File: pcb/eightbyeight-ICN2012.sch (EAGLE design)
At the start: 135 parts, among them J1 USB_MICROSMT+THRUHULE, J2 JTAG_ARM_10PIN, J3 BATTERY, Q1 16MHz, SW1 SWITCH_SPDT, SW2 BRIGHTNESS, U1 MK20DN32VFM5, U2 ICN2026, U3 QMA6981, U4 ICN2026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

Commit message: Update board TODOs
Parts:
- C16: value 470pF -> 47pF
- C6: value 10uF -> 20uF
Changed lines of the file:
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@@
 <part name="C12" library="adafruit" deviceset="C-US" device="C0805" value="10uF"/>
 <part name="C9" library="adafruit" deviceset="C-US" device="C0805" value="10uF"/>
-<part name="C6" library="adafruit" deviceset="C-US" device="C0805" value="10uF"/>
+<part name="C6" library="adafruit" deviceset="C-US" device="C0805" value="20uF"/>
 <part name="GND38" library="SparkFun-Aesthetics" deviceset="GND" device=""/>
 <part name="GND39" library="SparkFun-Aesthetics" deviceset="GND" device=""/>
 <part name="U5" library="SparkFun-PowerIC" deviceset="V_REG_MIC5219" device="3.3V" value="MIC5219 3.3V"/>
-<part name="C16" library="adafruit" deviceset="C-US" device="C0402" value="470pF"/>
+<part name="C16" library="adafruit" deviceset="C-US" device="C0402" value="47pF"/>
 <part name="GND40" library="SparkFun-Aesthetics" deviceset="GND" device=""/>
 <part name="P+1" library="supply1" deviceset="+5V" device=""/>
@@
 -Test a flush-mount USB connector
 -Choose either 3V or 3.3V regulator and make consistent
--Add 5v test pad?</text>
+-Add 5v test pad?
+-Remove pullup resistor on button?</text>
 <text x="129.54" y="358.14" size="10.16" layer="91" align="bottom-center">EightByEight Blinky Badge</text>
 <text x="129.54" y="345.44" size="6.4516" layer="91" align="bottom-center">Copyright 2016 Blinkinlabs, LLC</text>

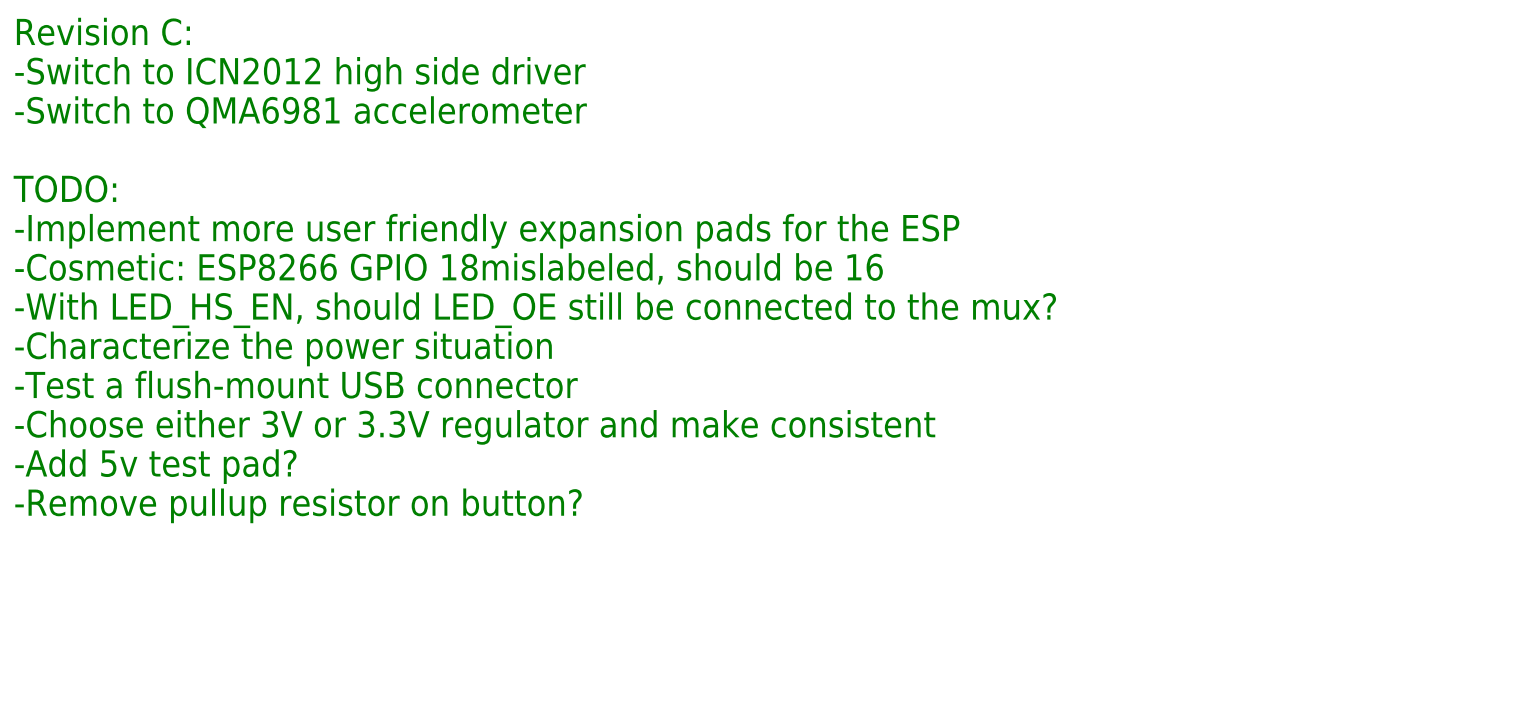
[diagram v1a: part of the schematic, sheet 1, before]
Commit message: Silkscreen tweaks to pcbs
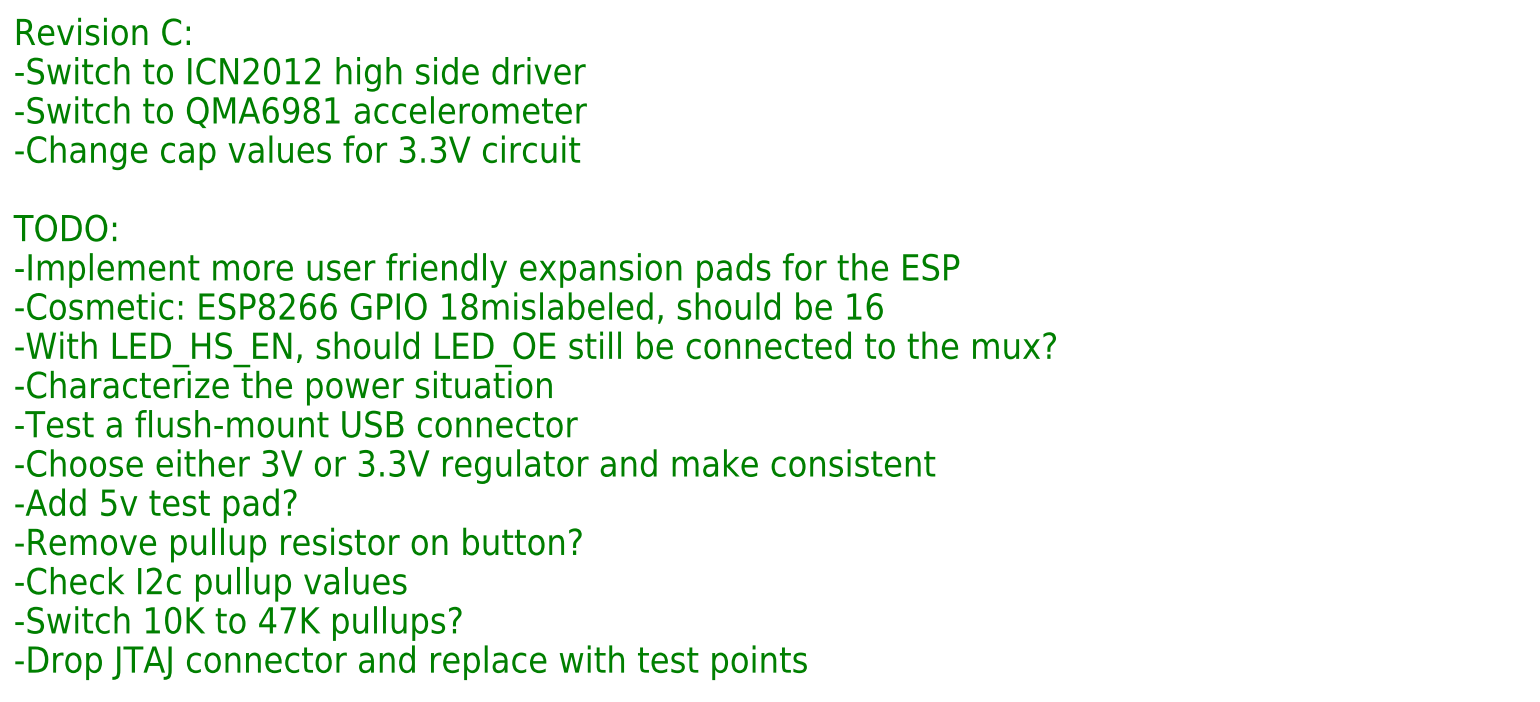
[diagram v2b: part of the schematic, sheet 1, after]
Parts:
- U2, U4: value ICN2026 -> ICN2027
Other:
- note added: "High side (row) driver"
- note removed: "High side (column) driver"
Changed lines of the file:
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@@
 </classes>
 <parts>
-<part name="U2" library="blinkinlabs" deviceset="ICN2026" device=""/>
+<part name="U2" library="blinkinlabs" deviceset="ICN2026" device="" value="ICN2027"/>
 <part name="GND2" library="SparkFun-Aesthetics" deviceset="GND" device=""/>
 <part name="C7" library="adafruit" deviceset="C-US" device="C0402" value="100nF"/>
@@
 <part name="R5" library="adafruit" deviceset="R-US_" device="R0402" value="2k"/>
 <part name="GND8" library="SparkFun-Aesthetics" deviceset="GND" device=""/>
-<part name="U4" library="blinkinlabs" deviceset="ICN2026" device=""/>
+<part name="U4" library="blinkinlabs" deviceset="ICN2026" device="" value="ICN2027"/>
 <part name="GND9" library="SparkFun-Aesthetics" deviceset="GND" device=""/>
 <part name="R9" library="adafruit" deviceset="R-US_" device="R0402" value="2k 1%"/>
@@
 -Switch to ICN2012 high side driver
 -Switch to QMA6981 accelerometer
+-Change cap values for 3.3V circuit
 TODO:
 -Implement more user friendly expansion pads for the ESP
@@
 -Choose either 3V or 3.3V regulator and make consistent
 -Add 5v test pad?
--Remove pullup resistor on button?</text>
+-Remove pullup resistor on button?
+-Check I2c pullup values
+-Switch 10K to 47K pullups?
+-Drop JTAJ connector and replace with test points</text>
 <text x="129.54" y="358.14" size="10.16" layer="91" align="bottom-center">EightByEight Blinky Badge</text>
 <text x="129.54" y="345.44" size="6.4516" layer="91" align="bottom-center">Copyright 2016 Blinkinlabs, LLC</text>
@@
 <wire x1="7.62" y1="101.6" x2="276.86" y2="101.6" width="0.4064" layer="94"/>
 <text x="12.7" y="71.12" size="1.778" layer="91">3 to 8 de-multiplexer with integrated P-MOSFETs</text>
-<text x="12.7" y="76.2" size="2.54" layer="94">High side (column) driver</text>
+<text x="12.7" y="76.2" size="2.54" layer="94">High side (row) driver</text>
 <wire x1="7.62" y1="83.82" x2="274.32" y2="83.82" width="0.4064" layer="94"/>
 <wire x1="7.62" y1="7.62" x2="7.62" y2="83.82" width="0.4064" layer="94"/>
@@
 <instances>
 <instance part="FRAME4" gate="G$1" x="0" y="0"/>
-<instance part="U2" gate="G$1" x="111.76" y="198.12"/>
+<instance part="U2" gate="G$1" x="111.76" y="198.12" smashed="yes"/>
 <instance part="GND2" gate="1" x="93.98" y="213.36"/>
 <instance part="C7" gate="G$1" x="17.78" y="220.98"/>
@@
 <instance part="GND4" gate="1" x="93.98" y="175.26"/>
 <instance part="R6" gate="G$1" x="17.78" y="180.34" rot="R90"/>
-<instance part="U4" gate="G$1" x="111.76" y="134.62"/>
+<instance part="U4" gate="G$1" x="111.76" y="134.62" smashed="yes"/>
 <instance part="GND9" gate="1" x="93.98" y="149.86"/>
 <instance part="R9" gate="G$1" x="93.98" y="121.92" rot="R90"/>

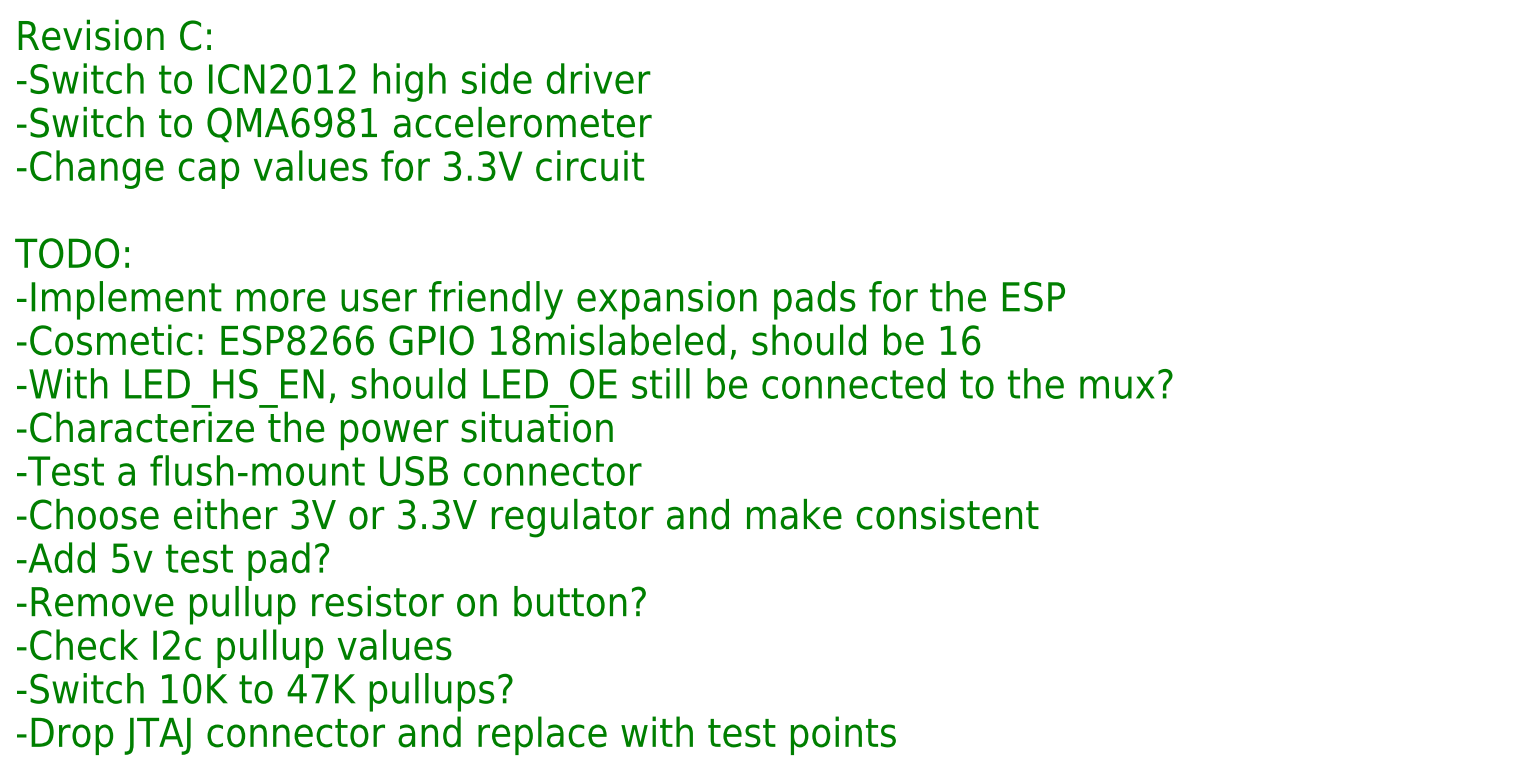
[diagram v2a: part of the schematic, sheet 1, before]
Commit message: Add (nonworking) RevC design
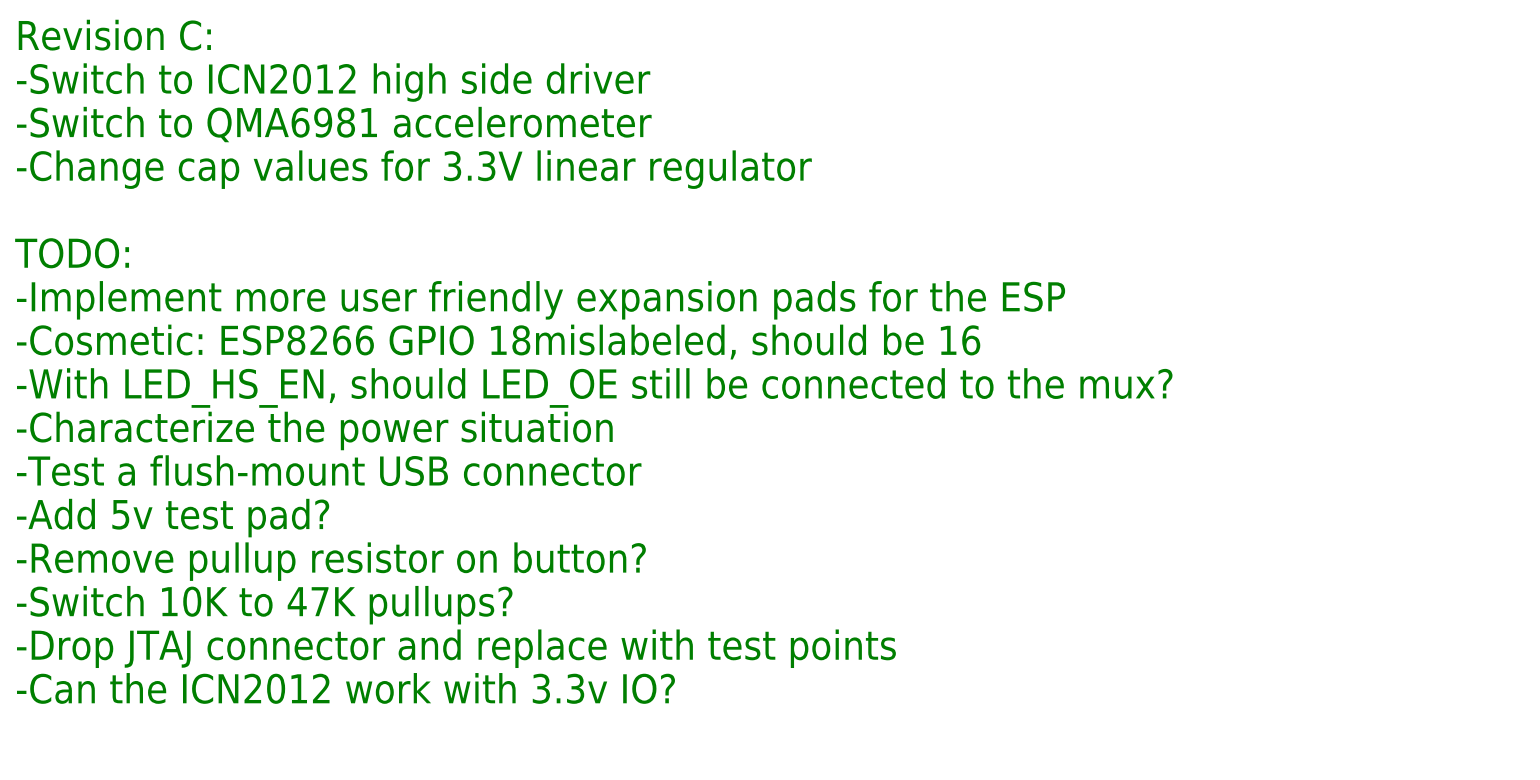
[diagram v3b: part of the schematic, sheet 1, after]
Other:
- note added: "Pin assignments for matrix output: LED_DAT + LED_CLK use ESPI0 LED_ROW_* and LED_STB need to be together on a unique port LED_OE needs to be on a pin with FTM capability"
- note removed: "Pin assignments for matrix output: LED_DAT + LED_CLK need to be together on a unique port LED_ROW_* and LED_STB need to be together on a unique port LED_OE needs to be on a pin with FTM capability"
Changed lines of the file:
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@@
 -Switch to ICN2012 high side driver
 -Switch to QMA6981 accelerometer
--Change cap values for 3.3V circuit
+-Change cap values for 3.3V linear regulator
 TODO:
 -Implement more user friendly expansion pads for the ESP
@@
 -Characterize the power situation
 -Test a flush-mount USB connector
--Choose either 3V or 3.3V regulator and make consistent
 -Add 5v test pad?
 -Remove pullup resistor on button?
--Check I2c pullup values
 -Switch 10K to 47K pullups?
--Drop JTAJ connector and replace with test points</text>
+-Drop JTAJ connector and replace with test points
+-Can the ICN2012 work with 3.3v IO?</text>
 <text x="129.54" y="358.14" size="10.16" layer="91" align="bottom-center">EightByEight Blinky Badge</text>
 <text x="129.54" y="345.44" size="6.4516" layer="91" align="bottom-center">Copyright 2016 Blinkinlabs, LLC</text>
@@
 <plain>
 <text x="76.2" y="101.6" size="1.778" layer="91">Pin assignments for matrix output:
-LED_DAT + LED_CLK need to be together on a unique port
+LED_DAT + LED_CLK use ESPI0
 LED_ROW_* and LED_STB need to be together on a unique port
 LED_OE needs to be on a pin with FTM capability</text>
